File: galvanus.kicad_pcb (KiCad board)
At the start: 2 copper layers, 69.8 x 35.6 mm, 26 parts, among them K1 CONN_3, K2 CONN_3, K3 CONN_3, K4 CONN_3, P1 CONN_6, P2 CONN_2, U1 SN74LV1T126, U10 MAX12931, U11 MAX12931, U12 MAX12931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

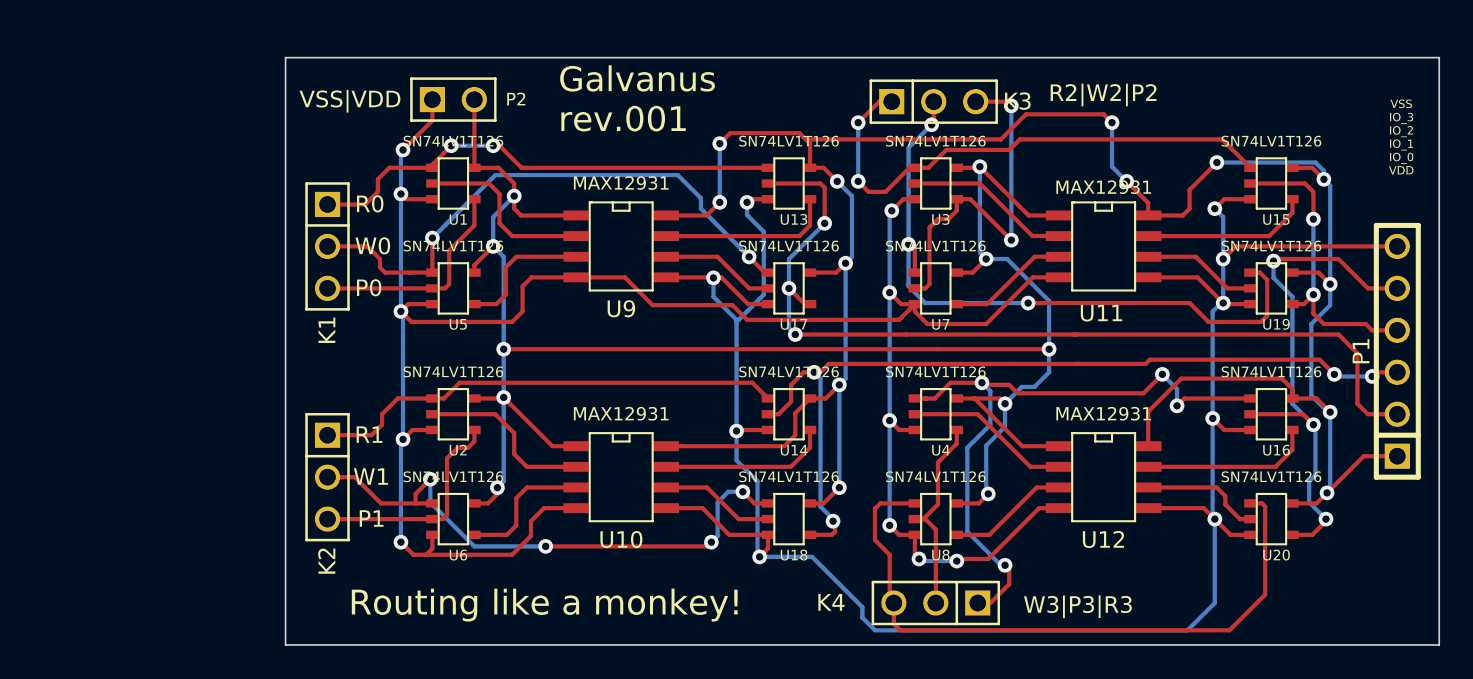
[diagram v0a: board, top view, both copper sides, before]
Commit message: Panelized PCB has been added
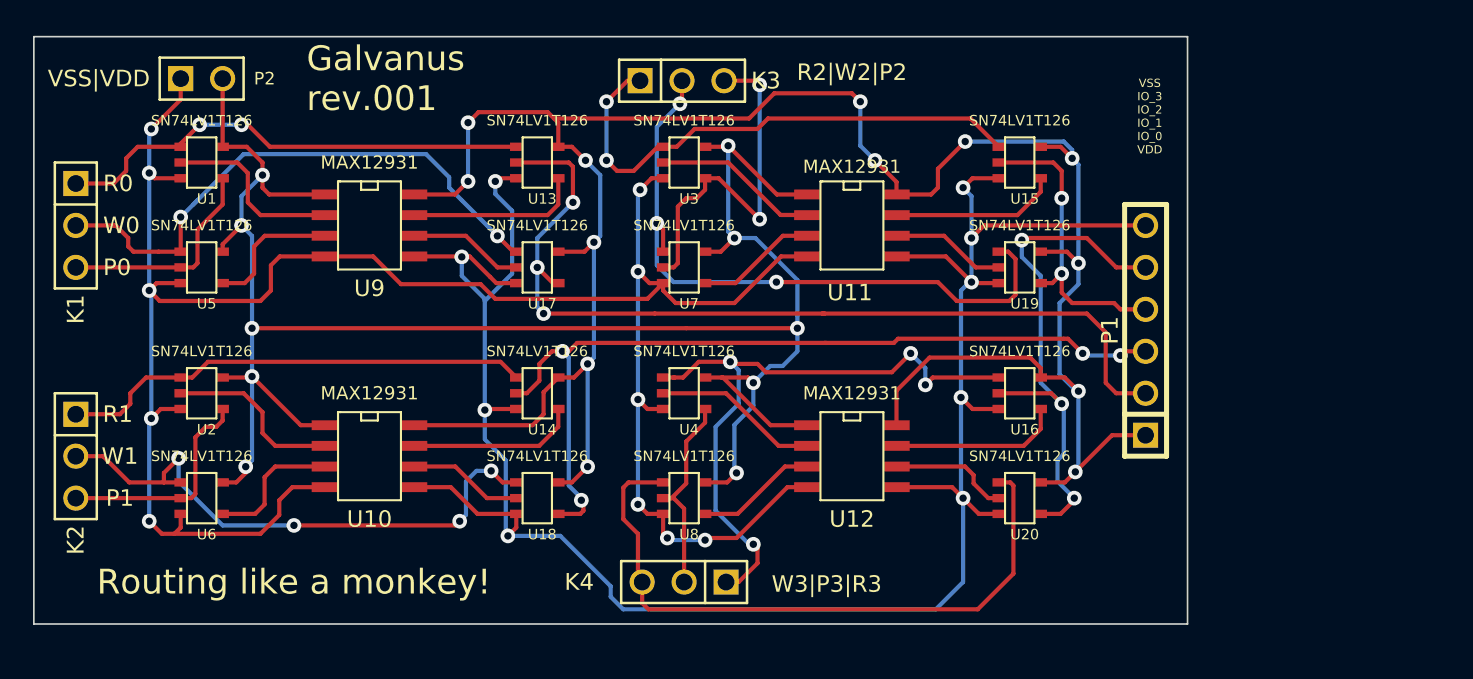
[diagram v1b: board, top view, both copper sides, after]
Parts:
- moved P1 15.3 mm to (82.5, 33.0)
- moved U11 15.3 mm to (64.8, 26.7)
- moved U12 15.3 mm to (64.8, 40.6)
- moved K1 15.3 mm to (17.8, 26.7)
- moved K2 15.3 mm to (17.8, 40.6)
- moved K3 15.3 mm to (54.5, 17.9)
- moved P2 15.3 mm to (25.4, 17.8)
- moved U1 15.3 mm to (25.4, 22.9)
- moved U13 15.3 mm to (45.7, 22.9)
- moved U14 15.3 mm to (45.7, 36.8)
- moved U17 15.3 mm to (45.7, 29.2)
- moved U18 15.3 mm to (45.7, 43.2)
- moved U2 15.3 mm to (25.4, 36.8)
- moved U5 15.3 mm to (25.4, 29.2)
- moved U6 15.3 mm to (25.4, 43.2)
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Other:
- board size 69.8 x 35.6 mm -> 69.9 x 35.6 mm
